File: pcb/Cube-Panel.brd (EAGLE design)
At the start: 100 x 100 mm, 139 parts, among them IC1 MBI5041-GP, IC2 ATTINY(261/461/861)V-MAZ

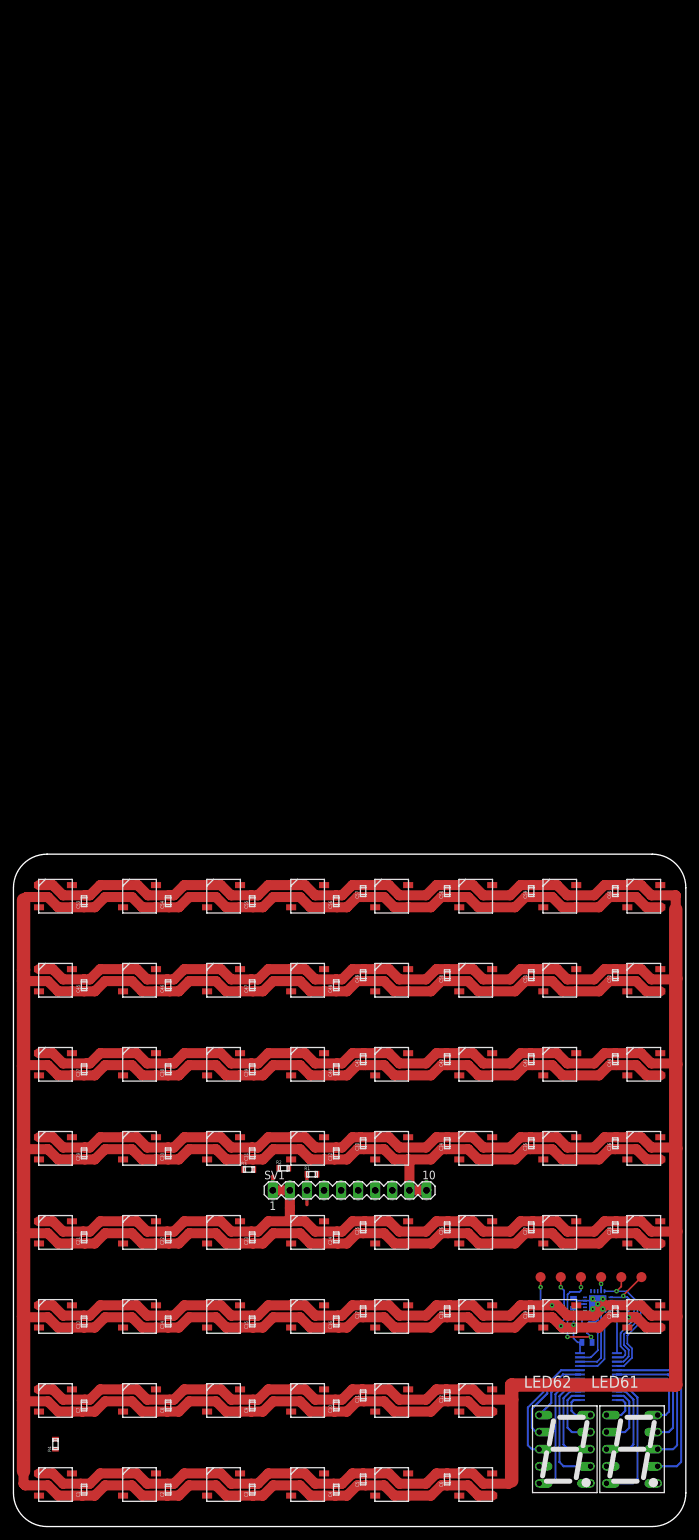
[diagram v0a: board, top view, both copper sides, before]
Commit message: Added resistors (0603) for path-configurability.
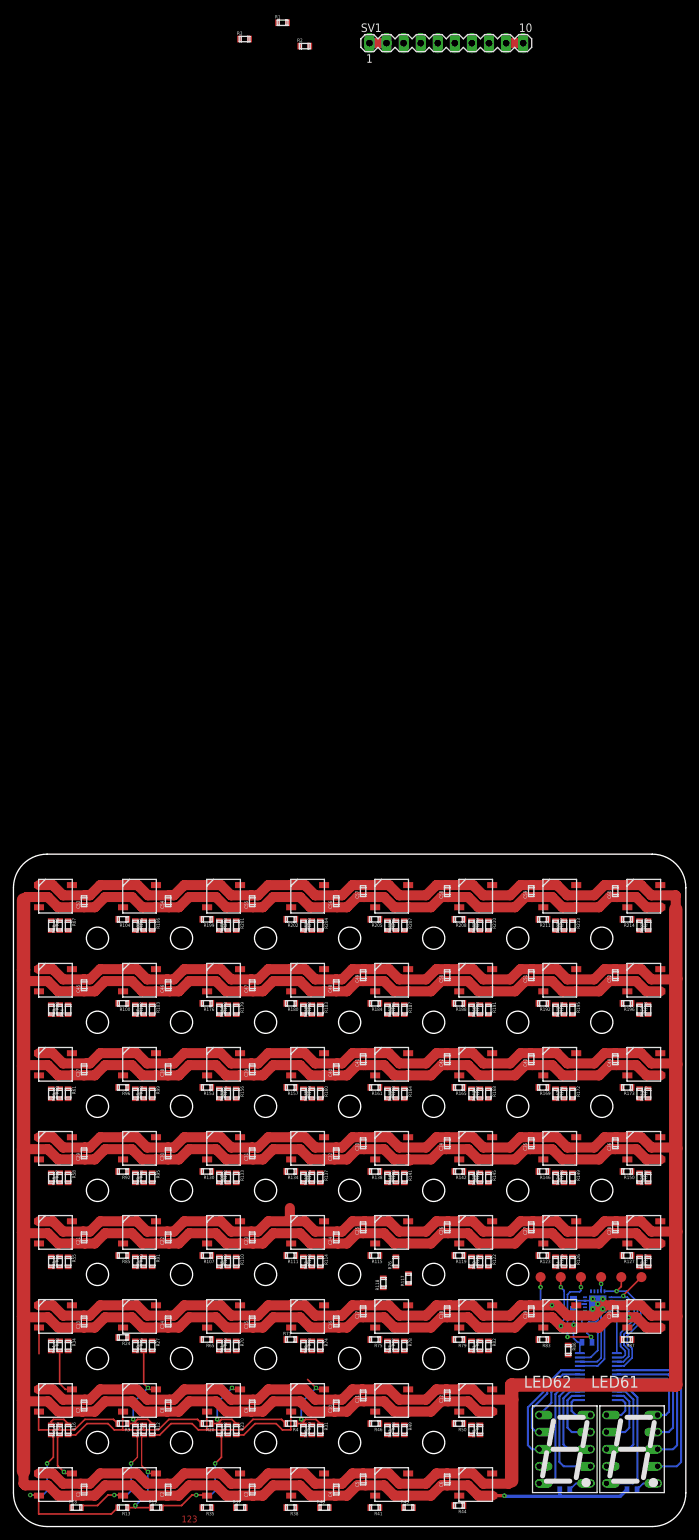
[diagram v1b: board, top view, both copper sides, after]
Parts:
- added R10, R100, R101, R102, R103, R104, R105, R106, R107, R108, R109, R11, R110, R111, R112, R113, R114, R115, R116, R117, R118, R119, R12, R120, R121, R122, R123, R124, R125, R126, R127, R128, R129, R13, R130, R131, R132, R133, R134, R135, R136, R137, R138, R139, R14, R140, R141, R142, R143, R144, R145, R146, R147, R148, R149, R15, R150, R151, R152, R153, R154, R155, R156, R157, R158, R159, R16, R160, R161, R162, R163, R164, R165, R166, R167, R168, R169, R17, R170, R171, R172, R173, R174, R175, R176, R177, R178, R179, R18, R180, R181, R182, R183, R184, R185, R186, R187, R188, R189, R19, R190, R191, R192, R193, R194, R195, R196, R197, R198, R199, R20, R200, R201, R202, R203, R204, R205, R206, R207, R208, R209, R21, R210, R211, R212, R213, R214, R215, R22, R23, R24, R25, R26, R27, R28, R29, R30, R31, R32, R33, R34, R35, R36, R37, R38, R39, R40, R41, R42, R43, R44, R45, R46, R47, R48, R49, R50, R51, R52, R53, R54, R55, R56, R57, R58, R59, R60, R61, R62, R63, R64, R65, R66, R67, R68, R69, R7, R70, R71, R72, R73, R74, R75, R76, R77, R78, R79, R8, R80, R81, R82, R83, R84, R85, R86, R87, R88, R89, R9, R90, R91, R92, R93, R94, R95, R96, R97, R98, R99: (no value), _Passive:0603
- moved R1 171.3 mm to (-9.97, 173.7)
- moved SV1 171.2 mm to (14.4, 170.6)
- moved R3 168.1 mm to (-15.6, 171.2)
- moved R2 166.9 mm to (-6.67, 170.2)
- moved R4 35.1 mm to (-8.75, -34.7), turned to 180 degrees
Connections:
- new net IN1: LED1.DIN, R13.P$2, R15.P$2
- new net IN10: LED10.DIN, R23.P$2, R39.P$2, R46.P$2, R73.P$2
- new net IN11: LED11.DIN, R31.P$2, R42.P$2, R50.P$2, R77.P$2
- new net IN12: LED12.DIN, R45.P$2, R49.P$2, R81.P$2
- new net IN13: LED13.DIN, R14.P$2, R24.P$2, R54.P$2
- new net IN14: LED14.DIN, R10.P$2, R34.P$2, R65.P$2, R90.P$2
- new net IN15: LED15.DIN, R109.P$2, R21.P$2, R27.P$2, R71.P$2
- new net IN16: LED16.DIN, R113.P$2, R29.P$2, R70.P$2, R75.P$2
- new net IN17: LED17.DIN, R117.P$2, R47.P$2, R74.P$2, R79.P$2
- new net IN18: LED18.DIN, R121.P$2, R51.P$2, R78.P$2, R83.P$2
- new net IN19: LED19.DIN, R125.P$2, R82.P$2, R87.P$2
- new net IN2: LED2.DIN, R11.P$2, R28.P$2, R35.P$2
- new net IN20: LED20.DIN, R129.P$2, R86.P$2
- new net IN21: LED21.DIN, R32.P$2, R57.P$2, R85.P$2
- new net IN22: LED22.DIN, R107.P$2, R25.P$2, R55.P$2, R94.P$2
- new net IN23: LED23.DIN, R111.P$2, R132.P$2, R68.P$2, R91.P$2
- new net IN24: LED24.DIN, R110.P$2, R115.P$2, R136.P$2, R72.P$2
- new net IN25: LED25.DIN, R114.P$2, R119.P$2, R140.P$2, R76.P$2
- new net IN26: LED26.DIN, R118.P$2, R123.P$2, R144.P$2, R80.P$2
- new net IN27: LED27.DIN, R122.P$2, R127.P$2, R148.P$2, R84.P$2
- new net IN28: LED28.DIN, R126.P$2, R152.P$2, R88.P$2
- new net IN29: LED29.DIN, R53.P$2, R60.P$2, R92.P$2
- new net IN3: LED3.DIN, R19.P$2, R22.P$2, R38.P$2
- new net IN30: LED30.DIN, R130.P$2, R58.P$2, R89.P$2, R98.P$2
- new net IN31: LED31.DIN, R108.P$2, R134.P$2, R155.P$2, R95.P$2
- new net IN32: LED32.DIN, R112.P$2, R133.P$2, R138.P$2, R159.P$2
- new net IN33: LED33.DIN, R116.P$2, R137.P$2, R142.P$2, R163.P$2
- new net IN34: LED34.DIN, R120.P$2, R141.P$2, R146.P$2, R167.P$2
- new net IN35: LED35.DIN, R124.P$2, R145.P$2, R150.P$2, R171.P$2
- new net IN36: LED36.DIN, R128.P$2, R149.P$2, R175.P$2
- new net IN37: LED37.DIN, R56.P$2, R63.P$2, R96.P$2
- new net IN38: LED38.DIN, R102.P$2, R153.P$2, R61.P$2, R93.P$2
- new net IN39: LED39.DIN, R131.P$2, R157.P$2, R178.P$2, R99.P$2
- new net IN4: LED4.DIN, R30.P$2, R37.P$2, R41.P$2
- new net IN40: LED40.DIN, R135.P$2, R156.P$2, R161.P$2, R182.P$2
- new net IN41: LED41.DIN, R139.P$2, R160.P$2, R165.P$2, R186.P$2
- new net IN42: LED42.DIN, R143.P$2, R164.P$2, R169.P$2, R190.P$2
- new net IN43: LED43.DIN, R147.P$2, R168.P$2, R173.P$2, R194.P$2
- new net IN44: LED44.DIN, R151.P$2, R172.P$2, R198.P$2
- new net IN45: LED45.DIN, R100.P$2, R59.P$2, R66.P$2
- new net IN46: LED46.DIN, R105.P$2, R176.P$2, R64.P$2, R97.P$2
- new net IN47: LED47.DIN, R103.P$2, R154.P$2, R180.P$2, R200.P$2
- new net IN48: LED48.DIN, R158.P$2, R179.P$2, R184.P$2, R203.P$2
- new net IN49: LED49.DIN, R162.P$2, R183.P$2, R188.P$2, R206.P$2
- new net IN5: LED5.DIN, R40.P$2, R44.P$2, R48.P$2
- new net IN50: LED50.DIN, R166.P$2, R187.P$2, R192.P$2, R209.P$2
- new net IN51: LED51.DIN, R170.P$2, R191.P$2, R196.P$2, R212.P$2
- new net IN52: LED52.DIN, R174.P$2, R195.P$2, R215.P$2
- new net IN53: LED53.DIN, R104.P$2, R62.P$2
- new net IN54: LED54.DIN, R101.P$2, R199.P$2, R67.P$2
- new net IN55: LED55.DIN, R106.P$2, R177.P$2, R202.P$2
- new net IN56: LED56.DIN, R181.P$2, R201.P$2, R205.P$2
- new net IN57: LED57.DIN, R185.P$2, R204.P$2, R208.P$2
- new net IN58: LED58.DIN, R189.P$2, R207.P$2, R211.P$2
- new net IN59: LED59.DIN, R193.P$2, R210.P$2, R214.P$2
- new net IN6: LED6.DIN, R43.P$2, R52.P$2
- new net IN60: LED60.DIN, R197.P$2, R213.P$2
- new net IN7: LED7.DIN, R18.P$2, R33.P$2, R9.P$2
- new net IN8: LED8.DIN, R16.P$2, R17.P$2, R20.P$2, R26.P$2
- new net IN9: LED9.DIN, R12.P$2, R36.P$2, R4.P$2, R69.P$2
- new net OUT1: LED1.DOUT, R18.P$1, R28.P$1
- new net OUT10: LED10.DOUT, R29.P$1, R30.P$1, R31.P$1, R4.P$1
- new net OUT11: LED11.DOUT, R46.P$1, R47.P$1, R48.P$1, R49.P$1
- new net OUT12: LED12.DOUT, R50.P$1, R51.P$1, R52.P$1
- new net OUT13: LED13.DOUT, R32.P$1, R33.P$1, R34.P$1
- new net OUT14: LED14.DOUT, R24.P$1, R25.P$1, R26.P$1, R27.P$1
- new net OUT15: LED15.DOUT, R65.P$1, R68.P$1, R69.P$1, R70.P$1
- new net OUT16: LED16.DOUT, R71.P$1, R72.P$1, R73.P$1, R74.P$1
- new net OUT17: LED17.DOUT, R75.P$1, R76.P$1, R77.P$1, R78.P$1
- new net OUT18: LED18.DOUT, R79.P$1, R80.P$1, R81.P$1, R82.P$1
- new net OUT19: LED19.DOUT, R83.P$1, R84.P$1, R86.P$1
- new net OUT2: LED2.DOUT, R13.P$1, R17.P$1, R19.P$1
- new net OUT20: LED20.DOUT, R87.P$1, R88.P$1
- new net OUT21: LED21.DOUT, R53.P$1, R54.P$1, R55.P$1
- new net OUT22: LED22.DOUT, R85.P$1, R89.P$1, R90.P$1, R91.P$1
- new net OUT23: LED23.DOUT, R107.P$1, R108.P$1, R109.P$1, R110.P$1
- new net OUT24: LED24.DOUT, R111.P$1, R112.P$1, R113.P$1, R114.P$1
- new net OUT25: LED25.DOUT, R115.P$1, R116.P$1, R117.P$1, R118.P$1, R119.P$1, R120.P$1, R121.P$1, R122.P$1
- new net OUT26: LED26.DOUT, R123.P$1, R124.P$1, R125.P$1, R126.P$1
- new net OUT27: LED27.DOUT, R127.P$1, R128.P$1, R129.P$1
- new net OUT28: LED28.DOUT
- new net OUT29: LED29.DOUT, R56.P$1, R57.P$1, R58.P$1
- new net OUT3: LED3.DOUT, R35.P$1, R36.P$1, R37.P$1
- new net OUT30: LED30.DOUT, R92.P$1, R93.P$1, R94.P$1, R95.P$1
- new net OUT31: LED31.DOUT, R130.P$1, R131.P$1, R132.P$1, R133.P$1
- new net OUT32: LED32.DOUT, R134.P$1, R135.P$1, R136.P$1, R137.P$1
- new net OUT33: LED33.DOUT, R138.P$1, R139.P$1, R140.P$1, R141.P$1
- new net OUT34: LED34.DOUT, R142.P$1, R143.P$1, R144.P$1, R145.P$1
- new net OUT35: LED35.DOUT, R146.P$1, R147.P$1, R148.P$1, R149.P$1
- new net OUT36: LED36.DOUT, R150.P$1, R151.P$1, R152.P$1
- new net OUT37: LED37.DOUT, R59.P$1, R60.P$1, R61.P$1
- new net OUT38: LED38.DOUT, R96.P$1, R97.P$1, R98.P$1, R99.P$1
- new net OUT39: LED39.DOUT, R153.P$1, R154.P$1, R155.P$1, R156.P$1
- new net OUT4: LED4.DOUT, R38.P$1, R39.P$1, R40.P$1
- new net OUT40: LED40.DOUT, R157.P$1, R158.P$1, R159.P$1, R160.P$1
- new net OUT41: LED41.DOUT, R161.P$1, R162.P$1, R163.P$1, R164.P$1
- new net OUT42: LED42.DOUT, R165.P$1, R166.P$1, R167.P$1, R168.P$1
- new net OUT43: LED43.DOUT, R169.P$1, R170.P$1, R171.P$1, R172.P$1
- new net OUT44: LED44.DOUT, R173.P$1, R174.P$1, R175.P$1
- new net OUT45: LED45.DOUT, R62.P$1, R63.P$1, R64.P$1
- new net OUT46: LED46.DOUT, R100.P$1, R101.P$1, R102.P$1, R103.P$1
- new net OUT47: LED47.DOUT, R176.P$1, R177.P$1, R178.P$1, R179.P$1
- new net OUT48: LED48.DOUT, R180.P$1, R181.P$1, R182.P$1, R183.P$1
- new net OUT49: LED49.DOUT, R184.P$1, R185.P$1, R186.P$1, R187.P$1
- new net OUT5: LED5.DOUT, R41.P$1, R42.P$1, R43.P$1
- new net OUT50: LED50.DOUT, R188.P$1, R189.P$1, R190.P$1, R191.P$1
- new net OUT51: LED51.DOUT, R192.P$1, R193.P$1, R194.P$1, R195.P$1
- new net OUT52: LED52.DOUT, R196.P$1, R197.P$1, R198.P$1
- new net OUT53: LED53.DOUT, R66.P$1, R67.P$1
- new net OUT54: LED54.DOUT, R104.P$1, R105.P$1, R106.P$1
- new net OUT55: LED55.DOUT, R199.P$1, R200.P$1, R201.P$1
- new net OUT56: LED56.DOUT, R202.P$1, R203.P$1, R204.P$1
- new net OUT57: LED57.DOUT, R205.P$1, R206.P$1, R207.P$1
- new net OUT58: LED58.DOUT, R208.P$1, R209.P$1, R210.P$1
- new net OUT59: LED59.DOUT, R211.P$1, R212.P$1, R213.P$1
- new net OUT6: LED6.DOUT, R44.P$1, R45.P$1
- new net OUT60: LED60.DOUT, R214.P$1, R215.P$1
- new net OUT7: LED7.DOUT, R14.P$1, R15.P$1, R16.P$1
- new net OUT8: LED8.DOUT, R10.P$1, R11.P$1, R12.P$1, R9.P$1
- new net OUT9: LED9.DOUT, R20.P$1, R21.P$1, R22.P$1, R23.P$1
- net N$26: now also R8.P$1
- net N$35: now also R7.P$1
- net VCC: now also R7.P$2, R8.P$2
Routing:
- net IN1: track 0.00 -> 27.8 mm, vias 0 -> 2
- net IN8: track 0.00 -> 25.4 mm
- net IN9: track 0.00 -> 24.6 mm
- net IN3: track 0.00 -> 19.5 mm, vias 0 -> 2
- net IN2: track 0.00 -> 18.6 mm, vias 0 -> 2
- net OUT8: track 0.00 -> 17.7 mm, vias 0 -> 2
- net VCC: track 909.3 -> 926.4 mm, vias 4 -> 5
- net OUT2: track 0.00 -> 16.9 mm, vias 0 -> 2
- net IN7: track 0.00 -> 16.2 mm
- net OUT10: track 0.00 -> 13.7 mm, vias 0 -> 2
- net OUT9: track 0.00 -> 12.1 mm, vias 0 -> 2
- net IN10: track 0.00 -> 12.0 mm
- net OUT7: track 0.00 -> 10.8 mm
- net OUT1: track 0.00 -> 7.31 mm, vias 0 -> 1
- net GND: track 940.6 -> 935.8 mm
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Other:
- board text added: "123"

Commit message: Added wired data-path resistors.
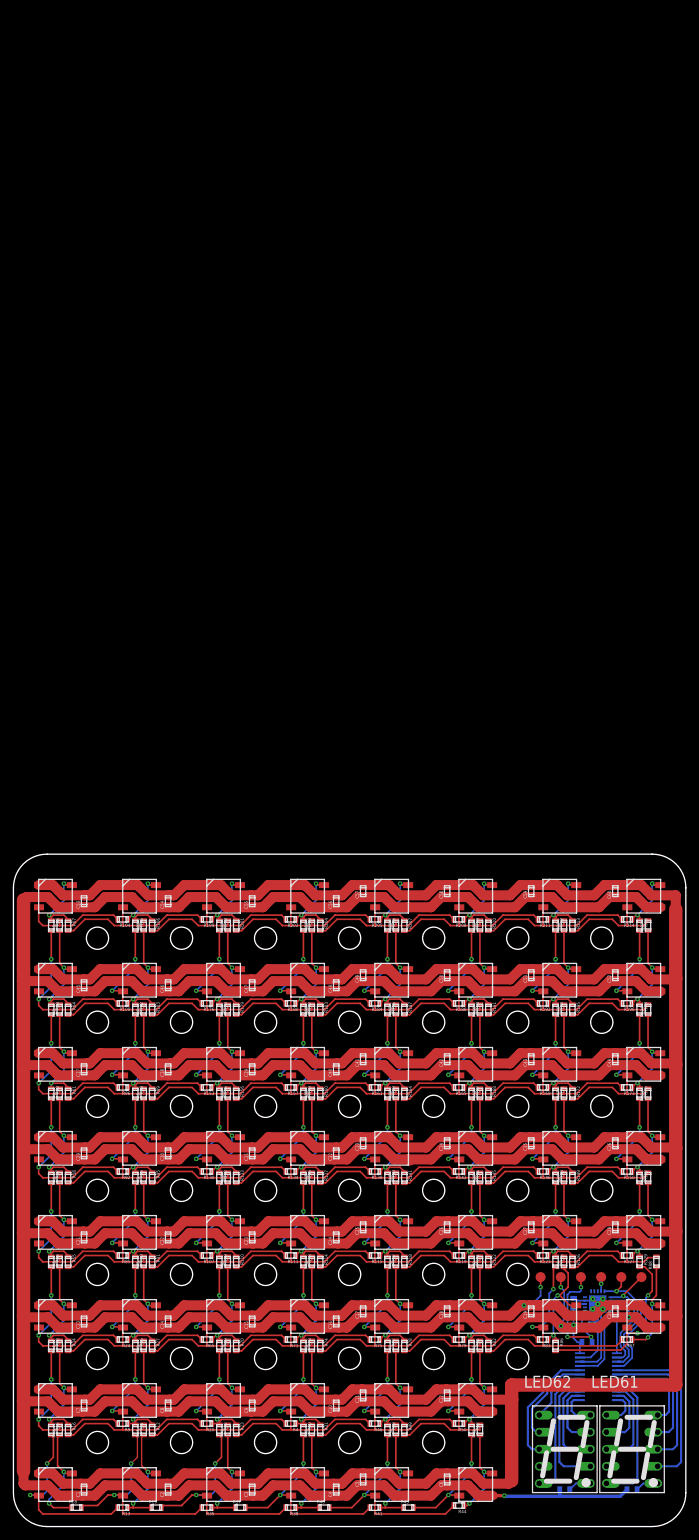
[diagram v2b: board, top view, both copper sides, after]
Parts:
- removed R1, R2, R3: (no value), _Passive:0603
- removed SV1: (no value), con-lstb:MA10-1
- moved R118 4.42 mm to (8.12, -10.6), turned to 270 degrees
- moved R117 4.00 mm to (5.62, -10.6), turned to 270 degrees
- moved R86 1.98 mm to (30.6, -23.1)
- moved R88 1.25 mm to (45.6, -10.6)
- moved R24 0.31 mm to (-33.8, -22.2)
- turned R64 to 270 degrees
- turned R71 to 180 degrees
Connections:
- removed net ID: R1.P$2, R2.P$2, SV1.3
- removed net N$1: R2.P$1, R3.P$2
- net GND: no longer R1.P$1, R3.P$1, SV1.1, SV1.2
- net OUT25: no longer R119.P$1, R120.P$1, R121.P$1, R122.P$1
- net OUT26: now also R119.P$1, R120.P$1, R121.P$1, R122.P$1; no longer R123.P$1, R124.P$1, R125.P$1, R126.P$1
- net OUT27: now also R123.P$1, R124.P$1, R125.P$1, R126.P$1; no longer R127.P$1, R128.P$1, R129.P$1
- net OUT28: now also R127.P$1, R128.P$1, R129.P$1
- net VCC: no longer SV1.10, SV1.9
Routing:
- net IN51: track 0.00 -> 37.4 mm, vias 0 -> 2
- net IN50: track 0.00 -> 37.4 mm, vias 0 -> 2
- net IN49: track 0.00 -> 37.4 mm, vias 0 -> 2
- net IN48: track 0.00 -> 37.4 mm, vias 0 -> 2
- net IN47: track 0.00 -> 37.4 mm, vias 0 -> 2
- net IN46: track 0.00 -> 37.4 mm, vias 0 -> 2
- net IN43: track 0.00 -> 37.4 mm, vias 0 -> 2
- net IN42: track 0.00 -> 37.4 mm, vias 0 -> 2
- net IN41: track 0.00 -> 37.4 mm, vias 0 -> 2
- net IN40: track 0.00 -> 37.4 mm, vias 0 -> 2
- net IN39: track 0.00 -> 37.4 mm, vias 0 -> 2
- net IN38: track 0.00 -> 37.4 mm, vias 0 -> 2
- net IN35: track 0.00 -> 37.4 mm, vias 0 -> 2
- net IN34: track 0.00 -> 37.4 mm, vias 0 -> 2
- net IN33: track 0.00 -> 37.4 mm, vias 0 -> 2
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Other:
- board text removed: "123"

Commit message: Added some labels and did some minor aesthetic corrections.
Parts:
- added R1, R2, R3: (no value), _Passive:0603
- added X2: JP8ER, jumper:JP8
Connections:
- new net BUS-RX: IC2.17
- new net BUS-TX: IC2.18
- new net N$1: R2.P$1, R3.P$2
- new net N$3: R1.P$2, R2.P$2, X2.6
- net GND: now also R1.P$1, R3.P$1, X2.7, X2.8
- net VCC: now also X2.1, X2.2
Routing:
- net N$4: track 0.00 -> 384.2 mm
- net GND: track 933.0 -> 985.2 mm
- net VCC: track 923.9 -> 966.0 mm
- net N$3: track 0.00 -> 5.39 mm
- net A2: track 13.6 -> 10.8 mm
- net H2: track 25.9 -> 23.9 mm
- net IN1: track 27.4 -> 25.5 mm
- net C2: track 21.8 -> 20.0 mm
- net B2: track 17.7 -> 15.9 mm
- net N$1: track 0.00 -> 1.25 mm
- net OUT2: track 17.0 -> 16.8 mm, vias 2 -> 3
- net OUT1: track 16.5 -> 16.2 mm, vias 2 -> 3
- net OUT25: track 17.7 -> 17.8 mm, vias 2 -> 3
- net OUT9: vias 2 -> 3
- net OUT8: vias 2 -> 3
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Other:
- board text added: "Alina"
- board text added: "ESCLAB 2021"
- board text added: "ID"
- board text added: "Jonathan"
- board text added: "Kevin"
- board text added: "Puzzle 1 Version 1.0"
- board text added: "Sanjeev"
